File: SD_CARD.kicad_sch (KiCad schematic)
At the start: 26 parts, among them J1 Micro_SD_Card_Det1

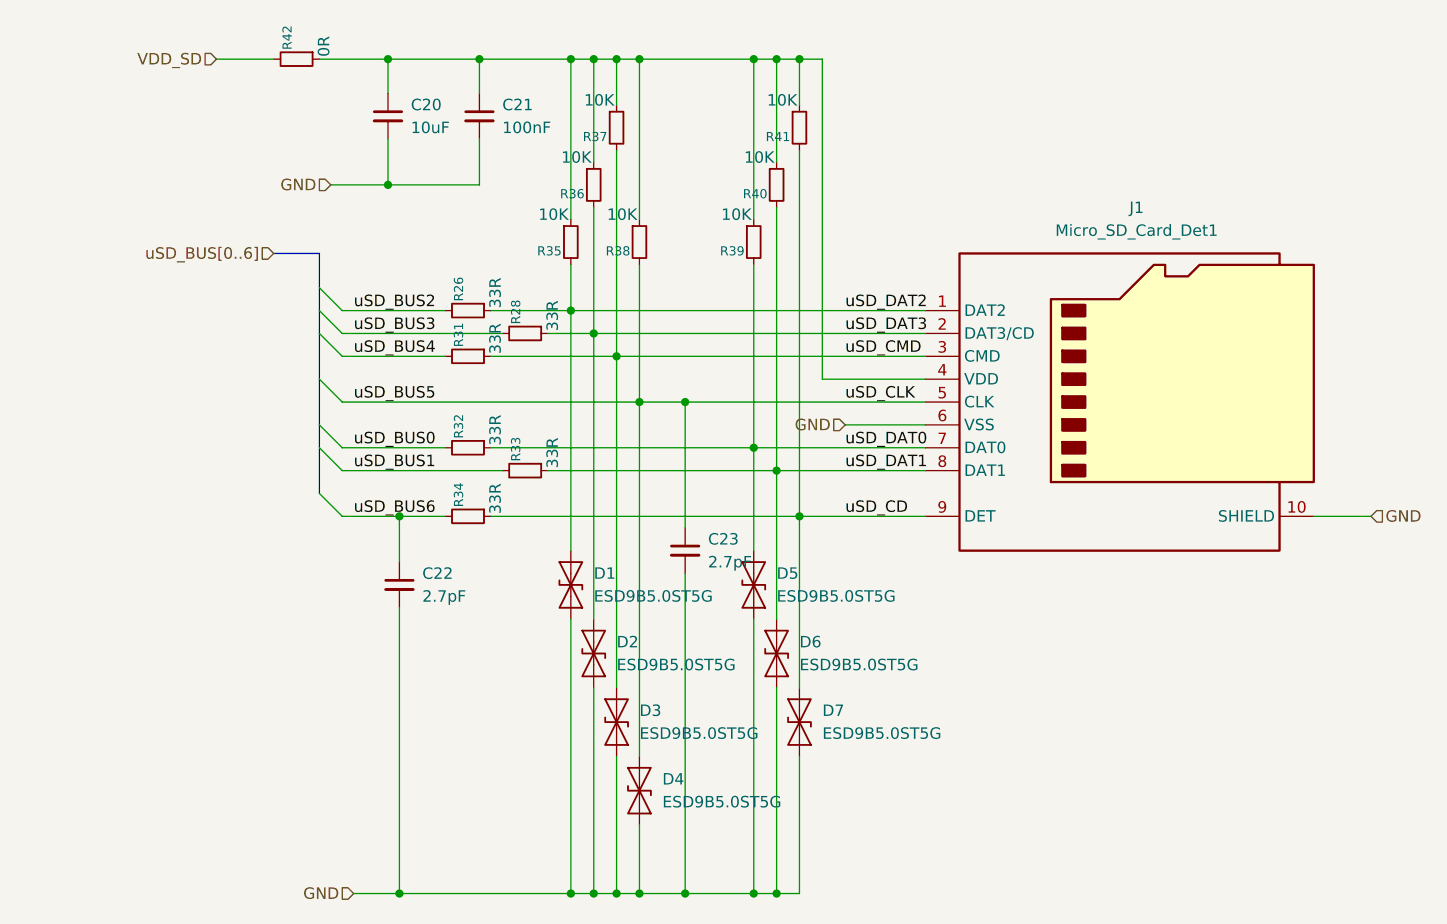
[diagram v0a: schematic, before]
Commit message: Completed ETH Module as per ref schematic also populated compatible busses in processor module
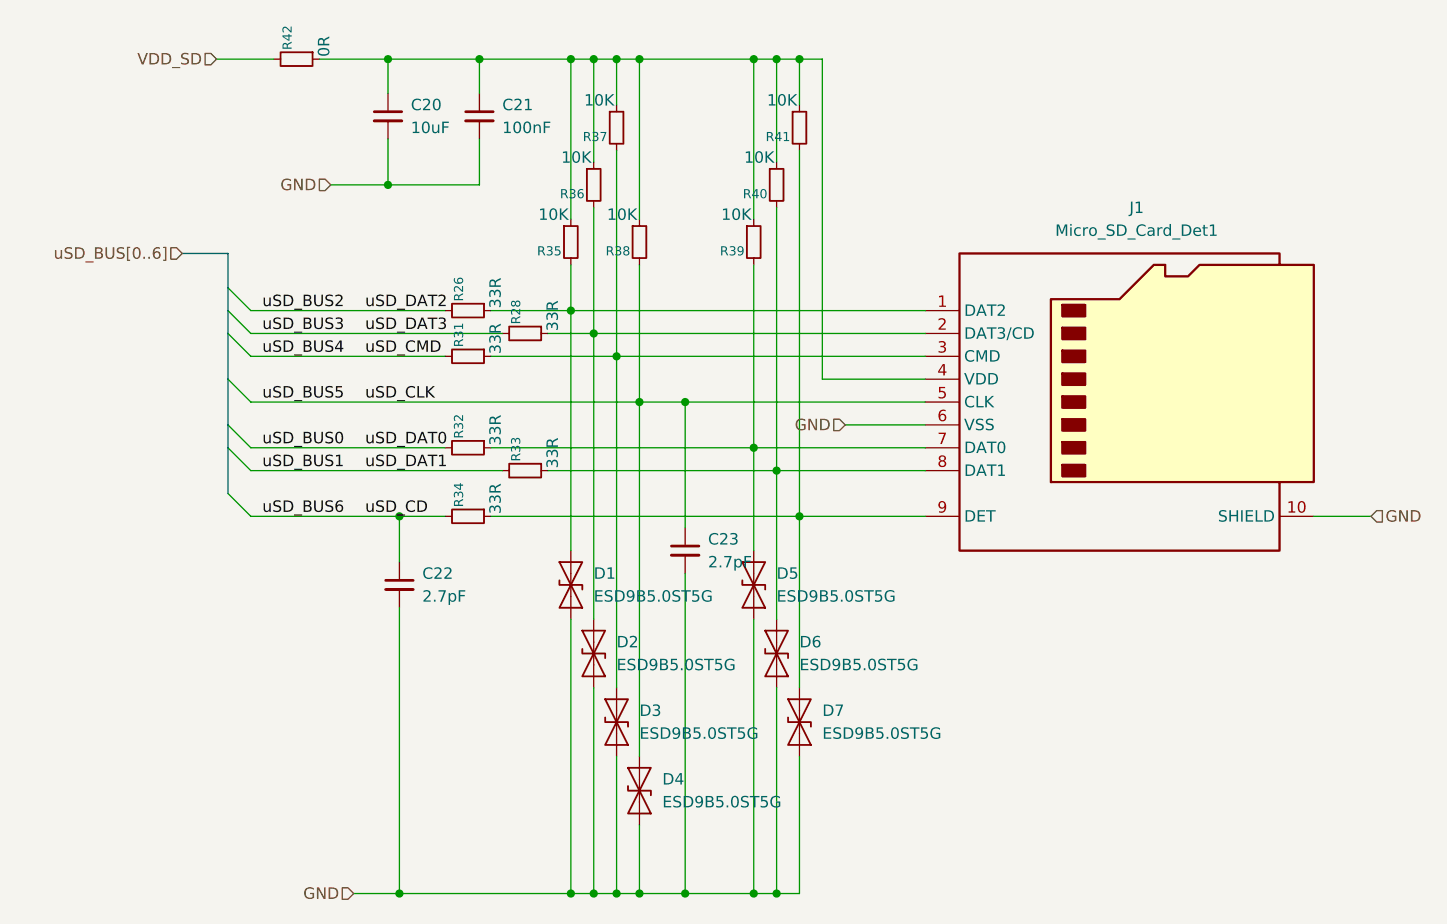
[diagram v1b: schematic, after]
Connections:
- net uSD_CD: no longer names the net of D7.2 (A2), J1.9 (DET), R34.1, R41.2
- net uSD_CMD: no longer names the net of D3.2 (A2), J1.3 (CMD), R31.1, R37.2
- net uSD_DAT0: no longer names the net of D5.2 (A2), J1.7 (DAT0), R32.1, R39.2
- net uSD_DAT1: no longer names the net of D6.2 (A2), J1.8 (DAT1), R33.1, R40.2
- net uSD_DAT2: no longer names the net of D1.2 (A2), J1.1 (DAT2), R26.1, R35.2
- net uSD_DAT3: no longer names the net of D2.2 (A2), J1.2 (DAT3/CD), R28.1, R36.2
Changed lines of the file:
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@@
 	)
 	(bus_entry
-		(at 71.12 90.17)
+		(at 60.96 90.17)
 		(size 2.54 2.54)
 		(stroke
@@
 	)
 	(bus_entry
-		(at 71.12 107.95)
+		(at 60.96 107.95)
 		(size 2.54 2.54)
 		(stroke
@@
 	)
 	(bus_entry
-		(at 71.12 95.25)
+		(at 60.96 95.25)
 		(size 2.54 2.54)
 		(stroke
@@
 	)
 	(bus_entry
-		(at 71.12 85.09)
+		(at 60.96 85.09)
 		(size 2.54 2.54)
 		(stroke
@@
 	)
 	(bus_entry
-		(at 71.12 100.33)
+		(at 60.96 100.33)
 		(size 2.54 2.54)
 		(stroke
@@
 	)
 	(bus_entry
-		(at 71.12 87.63)
+		(at 60.96 87.63)
 		(size 2.54 2.54)
 		(stroke
@@
 	)
 	(bus_entry
-		(at 71.12 102.87)
+		(at 60.96 102.87)
 		(size 2.54 2.54)
 		(stroke
@@
 	(wire
 		(pts
-			(xy 73.66 87.63) (xy 85.09 87.63)
+			(xy 63.5 87.63) (xy 85.09 87.63)
 		)
 		(stroke
@@
 	(wire
 		(pts
-			(xy 73.66 105.41) (xy 91.44 105.41)
+			(xy 63.5 105.41) (xy 91.44 105.41)
 		)
 		(stroke
@@
 	(wire
 		(pts
-			(xy 73.66 97.79) (xy 106.68 97.79)
+			(xy 63.5 97.79) (xy 106.68 97.79)
 		)
 		(stroke
@@
 	(bus
 		(pts
-			(xy 71.12 102.87) (xy 71.12 107.95)
+			(xy 60.96 102.87) (xy 60.96 107.95)
 		)
 		(stroke
@@
 	(wire
 		(pts
-			(xy 73.66 110.49) (xy 80.01 110.49)
+			(xy 63.5 110.49) (xy 80.01 110.49)
 		)
 		(stroke
@@
 	(bus
 		(pts
-			(xy 71.12 100.33) (xy 71.12 102.87)
+			(xy 60.96 100.33) (xy 60.96 102.87)
 		)
 		(stroke
@@
 	(bus
 		(pts
-			(xy 71.12 87.63) (xy 71.12 90.17)
+			(xy 60.96 87.63) (xy 60.96 90.17)
 		)
 		(stroke
@@
 	(wire
 		(pts
-			(xy 73.66 90.17) (xy 91.44 90.17)
+			(xy 63.5 90.17) (xy 91.44 90.17)
 		)
 		(stroke
@@
 	(bus
 		(pts
-			(xy 66.04 81.28) (xy 71.12 81.28)
+			(xy 55.88 81.28) (xy 60.96 81.28)
 		)
 		(stroke
@@
 	(bus
 		(pts
-			(xy 71.12 95.25) (xy 71.12 100.33)
+			(xy 60.96 95.25) (xy 60.96 100.33)
 		)
 		(stroke
@@
 	(bus
 		(pts
-			(xy 71.12 81.28) (xy 71.12 85.09)
+			(xy 60.96 81.28) (xy 60.96 85.09)
 		)
 		(stroke
@@
 	(bus
 		(pts
-			(xy 71.12 90.17) (xy 71.12 95.25)
+			(xy 60.96 90.17) (xy 60.96 95.25)
 		)
 		(stroke
@@
 	(wire
 		(pts
-			(xy 73.66 102.87) (xy 85.09 102.87)
+			(xy 63.5 102.87) (xy 85.09 102.87)
 		)
 		(stroke
@@
 	(wire
 		(pts
-			(xy 73.66 92.71) (xy 85.09 92.71)
+			(xy 63.5 92.71) (xy 85.09 92.71)
 		)
 		(stroke
@@
 	(bus
 		(pts
-			(xy 71.12 85.09) (xy 71.12 87.63)
+			(xy 60.96 85.09) (xy 60.96 87.63)
 		)
 		(stroke
@@
 	)
 	(label "uSD_DAT0"
-		(at 129.54 102.87 0)
+		(at 76.2 102.87 0)
 		(effects
 			(font
@@
 	)
 	(label "uSD_BUS4"
-		(at 74.93 92.71 0)
+		(at 64.77 92.71 0)
 		(effects
 			(font
@@
 	)
 	(label "uSD_CMD"
-		(at 129.54 92.71 0)
+		(at 76.2 92.71 0)
 		(effects
 			(font
@@
 	)
 	(label "uSD_BUS1"
-		(at 74.93 105.41 0)
+		(at 64.77 105.41 0)
 		(effects
 			(font
@@
 	)
 	(label "uSD_BUS6"
-		(at 74.93 110.49 0)
+		(at 64.77 110.49 0)
 		(effects
 			(font
@@
 	)
 	(label "uSD_CD"
-		(at 129.54 110.49 0)
+		(at 76.2 110.49 0)
 		(effects
 			(font
@@
 	)
 	(label "uSD_BUS5"
-		(at 74.93 97.79 0)
+		(at 64.77 97.79 0)
 		(effects
 			(font
@@
 	)
 	(label "uSD_CLK"
-		(at 129.54 97.79 0)
+		(at 76.2 97.79 0)
 		(effects
 			(font
@@
 	)
 	(label "uSD_BUS2"
-		(at 74.93 87.63 0)
+		(at 64.77 87.63 0)
 		(effects
 			(font
@@
 	)
 	(label "uSD_BUS0"
-		(at 74.93 102.87 0)
+		(at 64.77 102.87 0)
 		(effects
 			(font
@@
 	)
 	(label "uSD_DAT2"
-		(at 129.54 87.63 0)
+		(at 76.2 87.63 0)
 		(effects
 			(font
@@
 	)
 	(label "uSD_DAT3"
-		(at 129.54 90.17 0)
+		(at 76.2 90.17 0)
 		(effects
 			(font
@@
 	)
 	(label "uSD_DAT1"
-		(at 129.54 105.41 0)
+		(at 76.2 105.41 0)
 		(effects
 			(font
@@
 	)
 	(label "uSD_BUS3"
-		(at 74.93 90.17 0)
+		(at 64.77 90.17 0)
 		(effects
 			(font
@@
 	(hierarchical_label "uSD_BUS[0..6]"
 		(shape input)
-		(at 66.04 81.28 180)
-		(effects
-			(font
+		(at 55.88 81.28 180)
+		(effects
+			(font

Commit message: Updated Processor With ETH Pins
Also updated Capacitors and Resistors to 402
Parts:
- C20, C22: footprint Capacitor_SMD:C_0805_2012Metric -> Capacitor_SMD:C_0402_1005Metric
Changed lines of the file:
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@@
 			)
 		)
-		(property "Footprint" "Capacitor_SMD:C_0805_2012Metric"
+		(property "Footprint" "Capacitor_SMD:C_0402_1005Metric"
 			(at 78.74 66.04 0)
 			(effects
@@
 			)
 		)
-		(property "Footprint" "Capacitor_SMD:C_0805_2012Metric"
+		(property "Footprint" "Capacitor_SMD:C_0402_1005Metric"
 			(at 80.01 118.11 0)
 			(effects
